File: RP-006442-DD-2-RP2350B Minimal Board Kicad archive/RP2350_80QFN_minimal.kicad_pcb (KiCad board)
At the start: 2 copper layers, 100 x 100 mm, 134 parts, among them J1 USB_C_Receptacle_USB2.0_16P, J2 Conn_02x19_Odd_Even, J3 Conn_02x09_Odd_Even, J4 Conn_01x03, J5 USB_C_Receptacle_USB2.0_16P, J6 Conn_01x05, SW1 SW_Push, SW10 SW_DIP_x08, SW2 SW_Push, SW3 SW_Push, SW4 SW_Push, SW5 SW_Push, SW6 SW_Push, SW7 SW_Push, SW8 SW_Push, U1 RP2350_80QFN, U10 74HC595, U11 74HC595, U2 NCP1117-3.3_SOT223, U3 W25Q128JVS, U4 DNF, U5 W25Q128JVS, U6 NCP1117-3.3_SOT223, U7 RP2350_60QFN, U8 HT16K33A-24SSOP, U9 CC56-12EWA, Y1 ABM8-272-T3, Y2 ABM8-272-T3

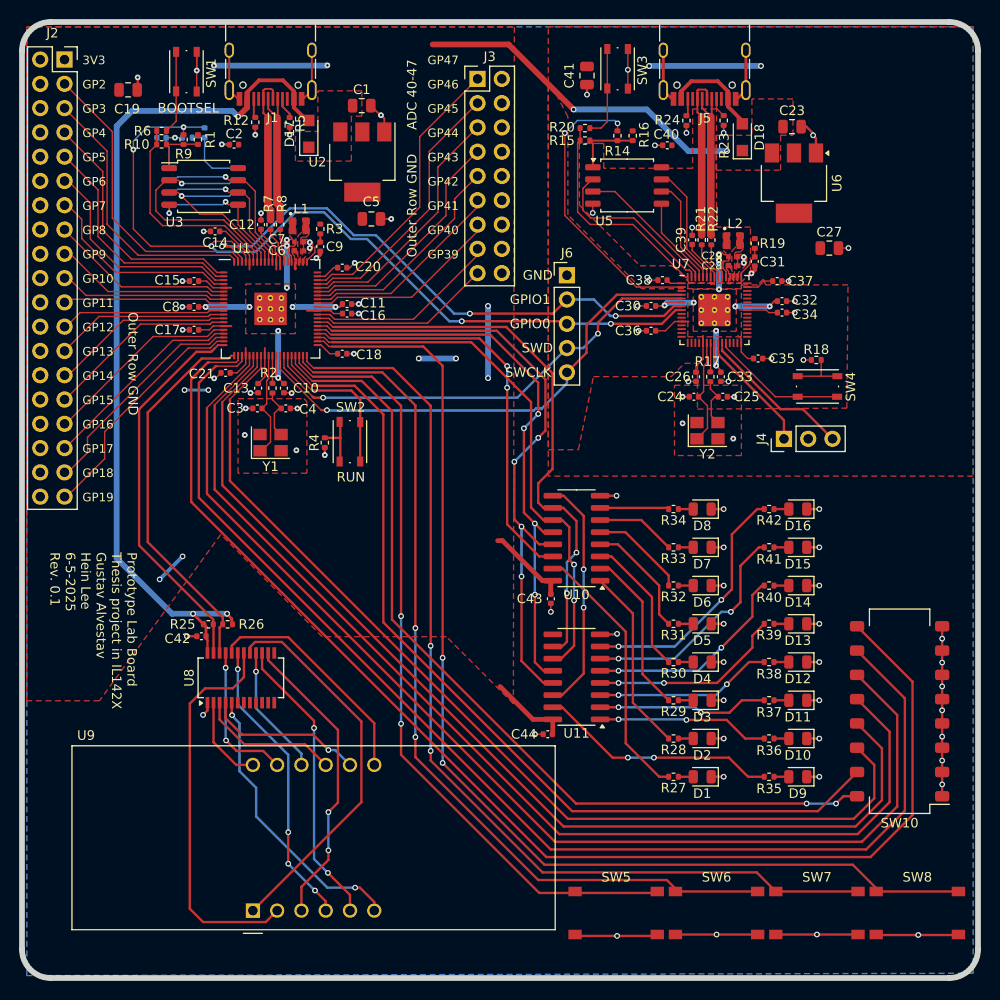
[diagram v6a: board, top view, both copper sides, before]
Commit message: Update accelerometer
Added accelerometer circuit to PCB editor
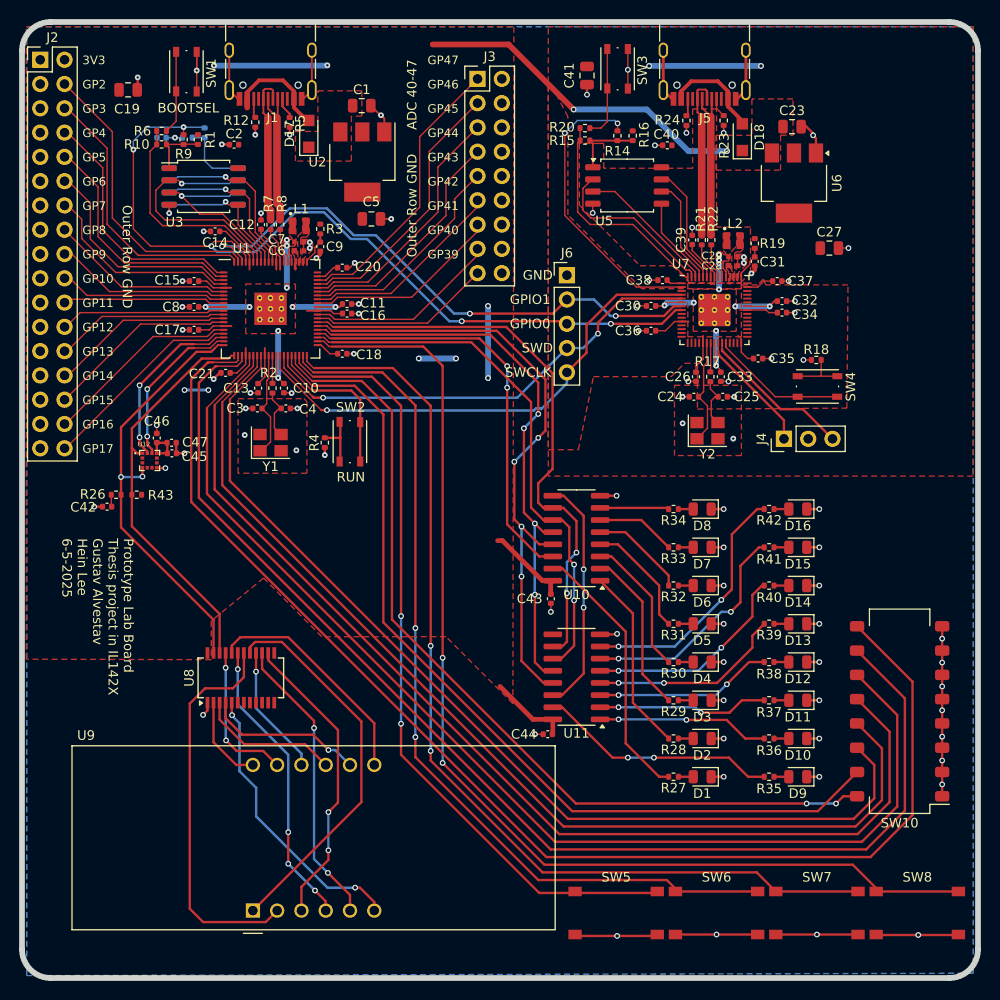
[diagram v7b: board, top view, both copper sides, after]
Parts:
- removed R25: 4.7k, Resistor_SMD:R_0402_1005Metric
- added C45: 100n, Capacitor_SMD:C_0402_1005Metric, F.Cu at (77.5, 90.2)
- added C46: 100n, Capacitor_SMD:C_0402_1005Metric, F.Cu at (76.0, 88.6)
- added C47: 10u, Capacitor_SMD:C_0402_1005Metric, F.Cu at (77.5, 89.1)
- added R43: 4.7k, Resistor_SMD:R_0402_1005Metric, F.Cu at (73.8, 94.5)
- added U12: LIS2DW12TR, LIS2DW12TR:LGA12R50P4X4_200X200X70, F.Cu at (75.2, 90.9)
- J2: value Conn_02x19_Odd_Even -> Conn_02x17_Odd_Even; footprint Connector_PinSocket_2.54mm:PinSocket_2x19_P2.54mm_Vertical -> Connector_PinHeader_2.54mm:PinHeader_2x17_P2.54mm_Vertical
- moved R26 17.9 mm to (71.7, 94.5), turned to 0 degrees
- moved C42 16.8 mm to (70.8, 95.8)
- moved J2 2.54 mm to (63.8, 49.0)
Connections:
- C1 pad 1: VDC -> Net-(D17-K)
- C42 pad 1: VBUS -> +3V3
- D17 pad 1: VDC -> Net-(D17-K)
- J2 pad 1: +3V3 -> GND
- J2 pad 10: GND -> /GPIO5
- J2 pad 11: /GPIO6 -> GND
- J2 pad 12: GND -> /GPIO6
- J2 pad 13: /GPIO7 -> GND
- J2 pad 14: GND -> /GPIO7
- J2 pad 15: /GPIO8 -> GND
- J2 pad 16: GND -> /GPIO8
- J2 pad 17: /GPIO9 -> GND
- J2 pad 18: GND -> /GPIO9
- J2 pad 19: /GPIO10 -> GND
- J2 pad 2: GND -> +3V3
- J2 pad 20: GND -> /GPIO10
- J2 pad 21: /GPIO11 -> GND
- J2 pad 22: GND -> /GPIO11
- J2 pad 23: /GPIO12 -> GND
- J2 pad 24: GND -> /GPIO12
- J2 pad 25: /GPIO13 -> GND
- J2 pad 26: GND -> /GPIO13
- J2 pad 27: /GPIO14 -> GND
- J2 pad 28: GND -> /GPIO14
- J2 pad 29: /GPIO15 -> GND
- J2 pad 3: /GPIO2 -> GND
- J2 pad 30: GND -> /GPIO15
- J2 pad 31: /GPIO16 -> GND
- J2 pad 32: GND -> /GPIO16
- J2 pad 33: /GPIO17 -> GND
- J2 pad 34: GND -> /GPIO17
- J2 pad 4: GND -> /GPIO2
- J2 pad 5: /GPIO3 -> GND
- J2 pad 6: GND -> /GPIO3
- J2 pad 7: /GPIO4 -> GND
- J2 pad 8: GND -> /GPIO4
- J2 pad 9: /GPIO5 -> GND
- R26 pad 1: VBUS -> +3V3
- R26 pad 2: /GPIO21 -> /GPIO20
- U2 pad 3: VDC -> Net-(D17-K)
- U8 pad 24: VBUS -> +3V3
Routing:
- net VBUS: track 102.0 -> 21.9 mm, vias 3 -> 0
- net /GPIO19: track 25.1 -> 17.0 mm, vias 0 -> 2
- net /GPIO18: track 23.5 -> 18.3 mm, vias 0 -> 2
- net /GPIO20: track 40.4 -> 45.1 mm, vias 0 -> 2
- net Net-(U12-VDD_IO): track 0.00 -> 4.34 mm
- net GND: track 155.4 -> 159.0 mm, vias 87 -> 90
- net /GPIO21: track 40.1 -> 42.5 mm
- net +3V3: track 128.7 -> 126.6 mm, vias 13 -> 11
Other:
- board text added: "Prototype Lab Board Thesis project in IL142X Gustav Alvestav Hein Lee 6-5-2025"
- board text removed: "GP18"
- board text removed: "GP19"
- board text removed: "Prototype Lab Board Thesis project in IL142X Gustav Alvestav Hein Lee 6-5-2025 Rev. 0.1"

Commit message: Update RP2350_80QFN_minimal.kicad_pcb
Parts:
- moved R43 3.76 mm to (70.1, 94.5), turned to 0 degrees
- moved R26 1.95 mm to (70.1, 93.4)
- moved C42 0.70 mm to (70.0, 95.7)
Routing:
- net +3V3: track 126.6 -> 139.3 mm, vias 11 -> 15
- net /GPIO21: track 42.5 -> 45.2 mm, vias 0 -> 2
- net /GPIO20: track 45.1 -> 47.0 mm
- net GND: track 159.0 -> 160.0 mm
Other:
- board text added: "ADC 40-47 Outer Row GND"
- board text removed: "ADC 40-47"
